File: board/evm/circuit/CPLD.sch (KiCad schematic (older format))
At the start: 1 part

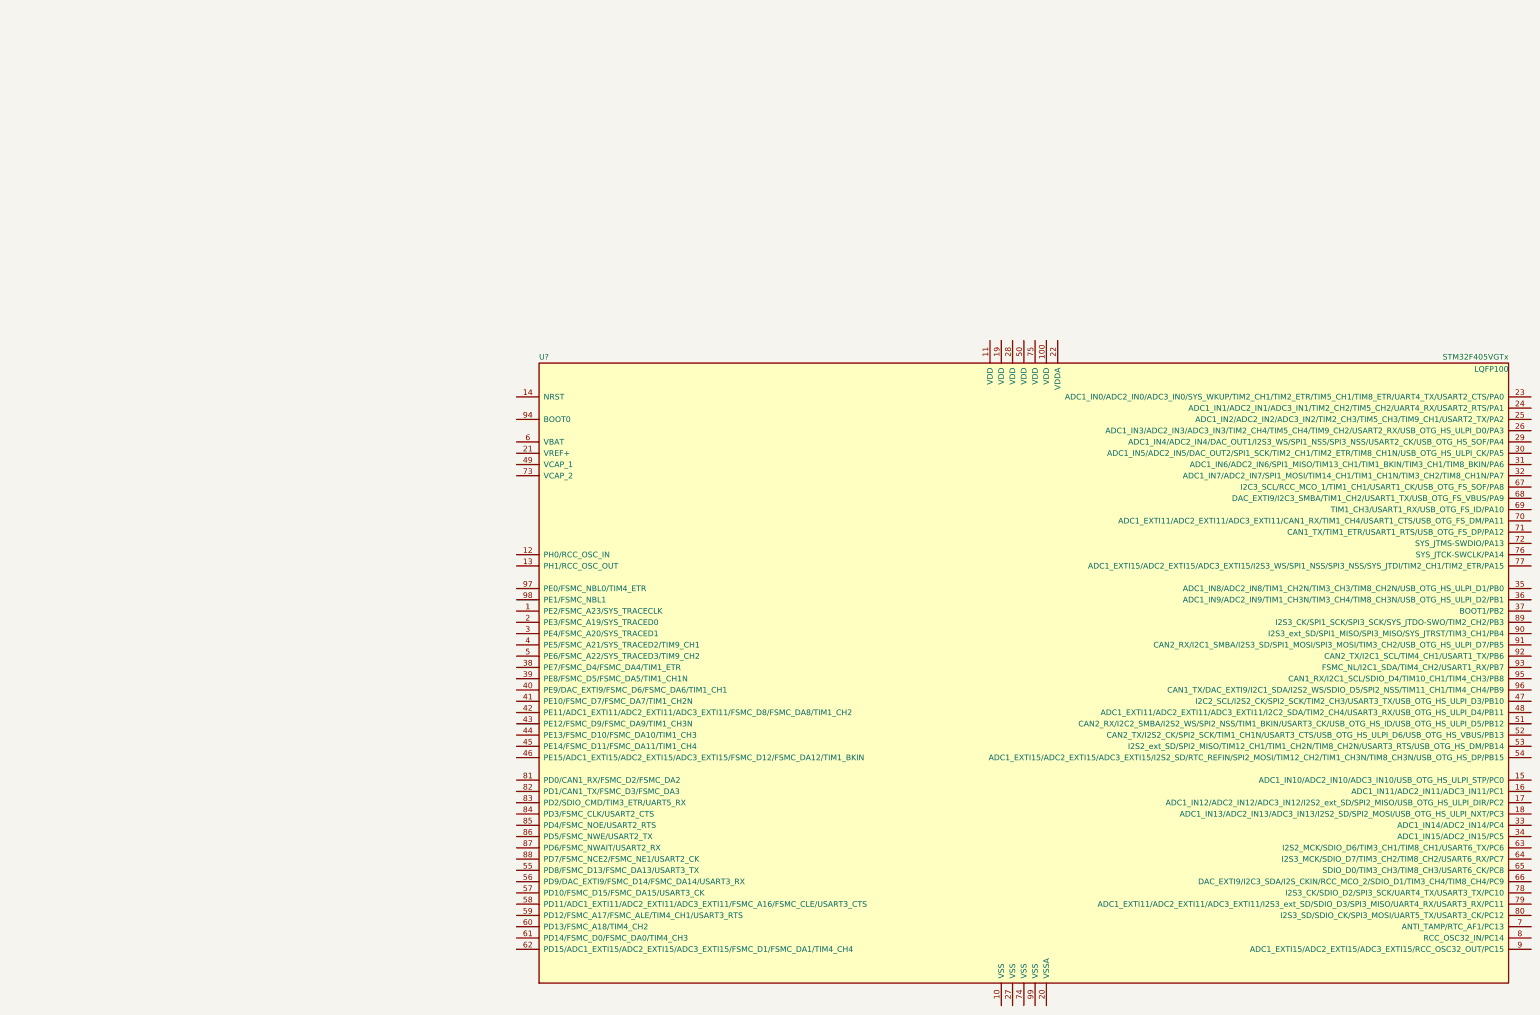
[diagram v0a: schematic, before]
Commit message: add cpld
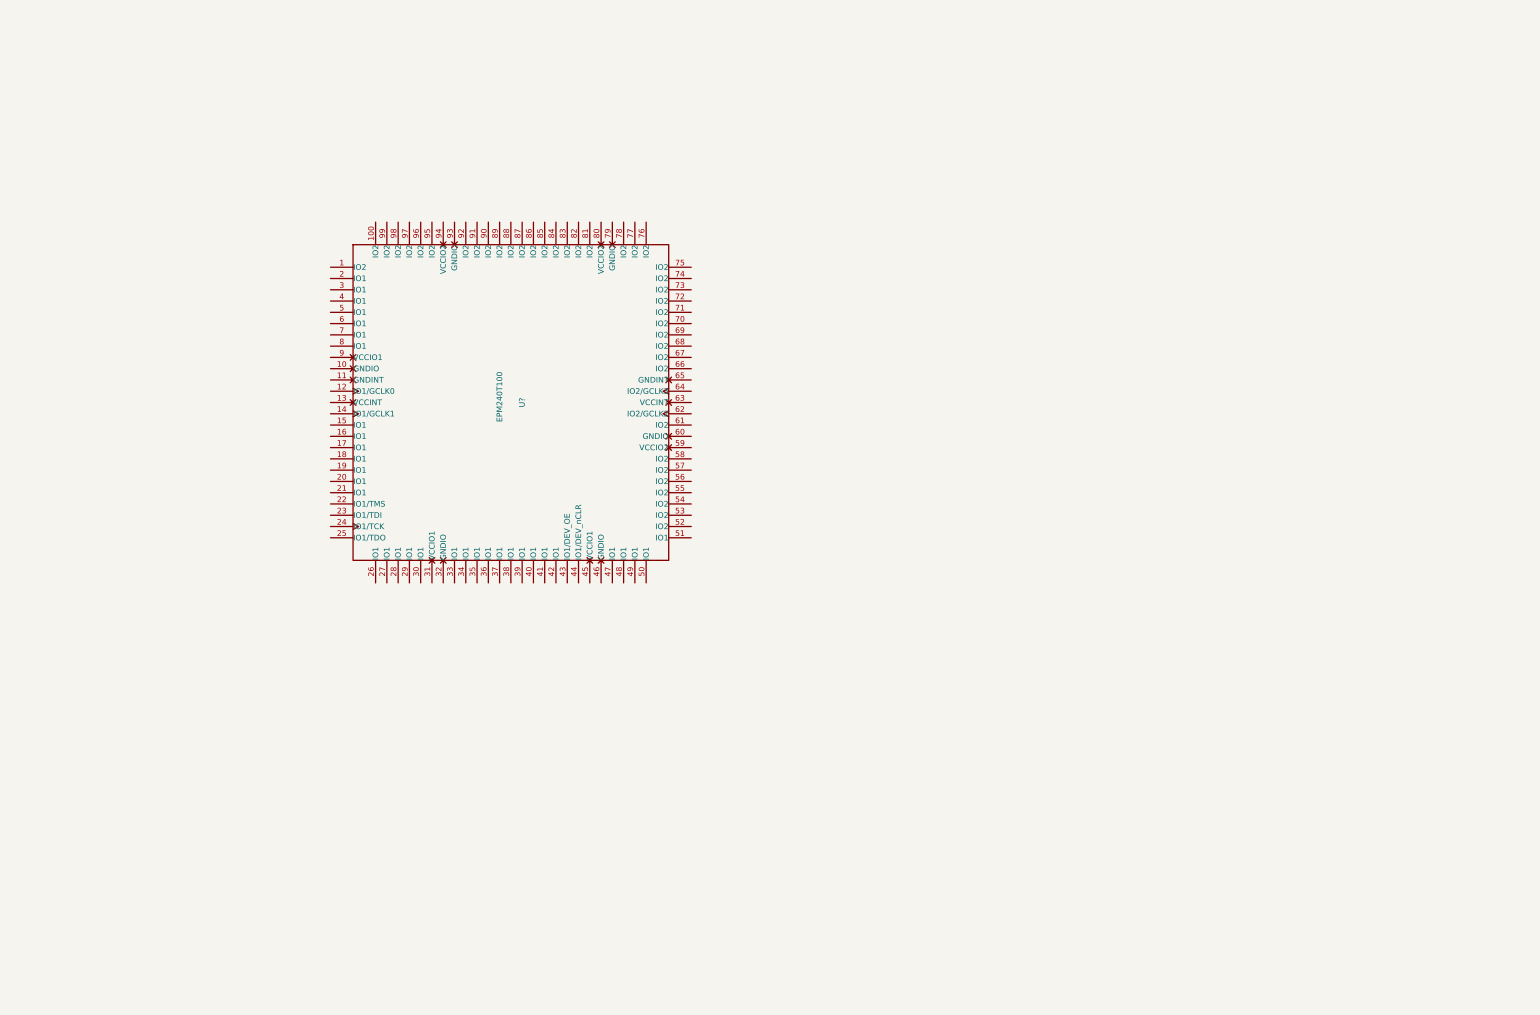
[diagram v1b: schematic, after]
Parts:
- removed U?: STM32F405VGTx, LQFP100, symbol STM32F405VGTx
- added U?: EPM240T100, symbol EPM240T100
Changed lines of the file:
@@
 $Descr A2 23386 16535
 encoding utf-8
-Sheet 2 4
+Sheet 4 4
 Title ""
 Date ""
@@
 $EndDescr
 $Comp
-L STM32F405VGTx U?
-U 1 1 5753F449
-P 9650 6400
-F 0 "U?" H 5350 9225 50  0000 L BNN
-F 1 "STM32F405VGTx" H 13950 9225 50  0000 R BNN
-F 2 "LQFP100" H 13950 9175 50  0000 R TNN
-F 3 "" H 9650 6400 50  0000 C CNN
-	1    9650 6400
+L EPM240T100 U?
+U 1 1 575650F8
+P 5100 3900
+F 0 "U?" V 5200 3850 50  0000 C CNN
+F 1 "EPM240T100" V 5000 3900 50  0000 C CNN
+F 2 "" V 4680 4400 30  0000 C CNN
+F 3 "" H 4750 4400 30  0000 C CNN
+	1    5100 3900
 	1    0    0    -1
 $EndComp

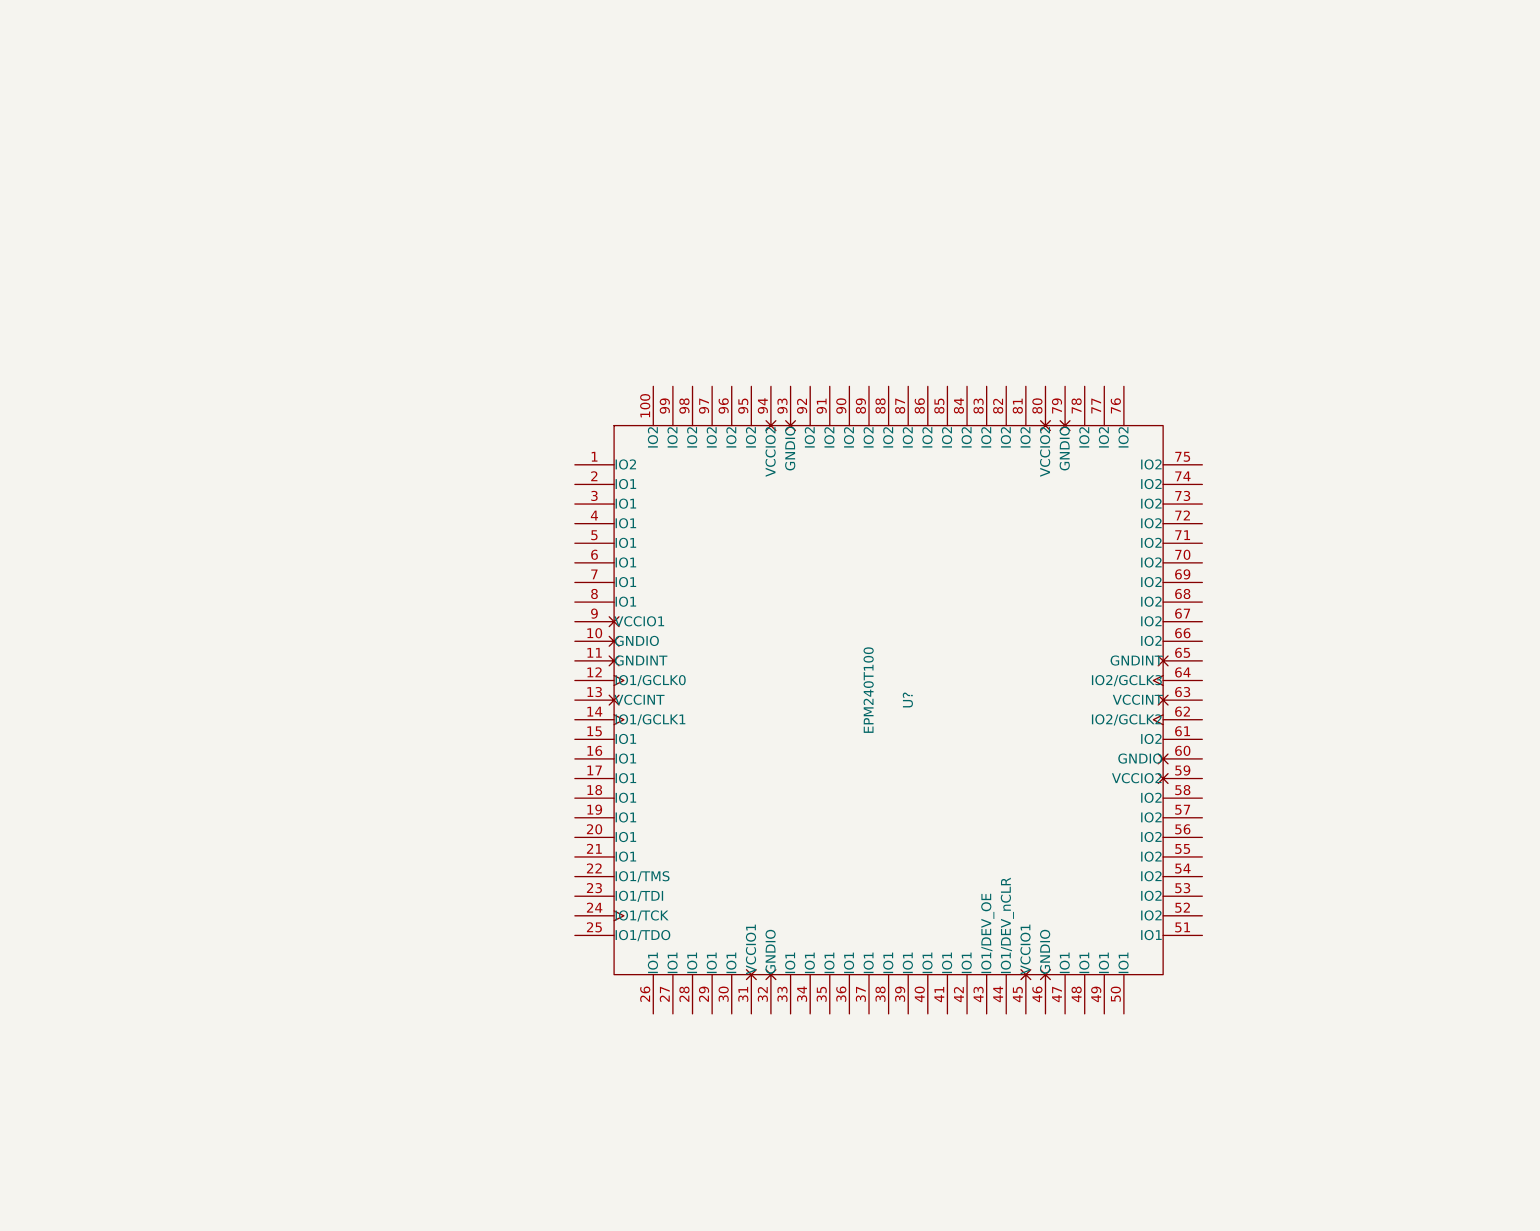
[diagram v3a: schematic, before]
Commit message: add more schs
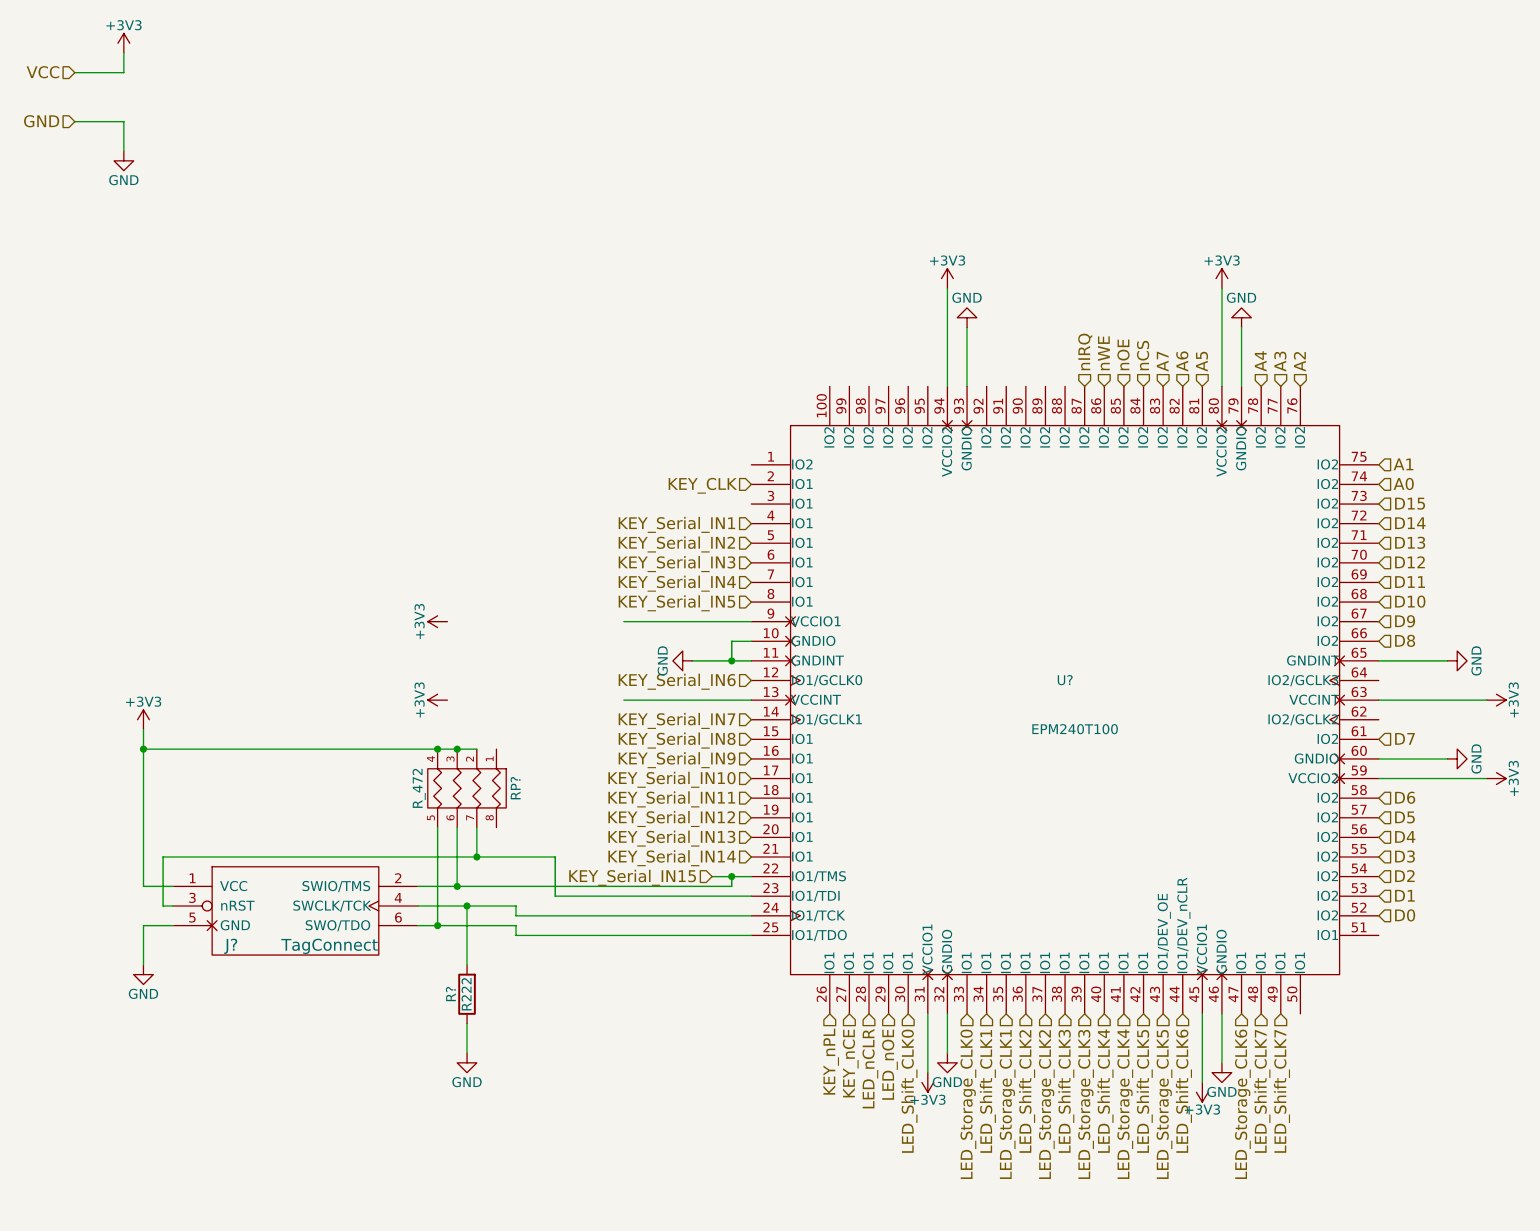
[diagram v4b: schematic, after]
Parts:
- added J?: TagConnect, symbol TagConnect
- added R?: R222, symbol R
- added RP?: R_472, symbol R_PACK4
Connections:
- net labels added: +3V3, A0, A1, A2, A3, A4, A5, A6, A7, D0, D1, D10, D11, D12, D13, D14, D15, D2, D3, D4, D5, D6, D7, D8, D9, GND, KEY_CLK, KEY_Serial_IN1, KEY_Serial_IN10, KEY_Serial_IN11, KEY_Serial_IN12, KEY_Serial_IN13, KEY_Serial_IN14, KEY_Serial_IN15, KEY_Serial_IN2, KEY_Serial_IN3, KEY_Serial_IN4, KEY_Serial_IN5, KEY_Serial_IN6, KEY_Serial_IN7, KEY_Serial_IN8, KEY_Serial_IN9, KEY_nCE, KEY_nPL, LED_Shift_CLK0, LED_Shift_CLK1, LED_Shift_CLK2, LED_Shift_CLK3, LED_Shift_CLK4, LED_Shift_CLK5, LED_Shift_CLK6, LED_Shift_CLK7, LED_Storage_CLK0, LED_Storage_CLK1, LED_Storage_CLK2, LED_Storage_CLK3, LED_Storage_CLK4, LED_Storage_CLK5, LED_Storage_CLK6, LED_nCLR, LED_nOE, VCC, nCS, nIRQ, nOE, nWE
- wire segments 0 -> 45
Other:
- moved on the sheet: U?

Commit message: evm sch design finished
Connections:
- net labels added: GPIO0, GPIO1, GPIO10, GPIO2, GPIO3, GPIO4, GPIO5, GPIO6, GPIO7, GPIO8, GPIO9
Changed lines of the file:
@@
 LIBS:contrib
 LIBS:valves
-LIBS:stm8
-LIBS:stm32
-LIBS:74xgxx
-LIBS:ac-dc
-LIBS:actel
 LIBS:Altera
-LIBS:analog_devices
-LIBS:battery_management
-LIBS:bbd
-LIBS:brooktre
-LIBS:cmos_ieee
-LIBS:dc-dc
-LIBS:diode
-LIBS:elec-unifil
-LIBS:ESD_Protection
-LIBS:ftdi
-LIBS:gennum
-LIBS:graphic
-LIBS:hc11
-LIBS:ir
-LIBS:Lattice
-LIBS:logo
-LIBS:maxim
-LIBS:microchip_dspic33dsc
-LIBS:microchip_pic10mcu
-LIBS:microchip_pic12mcu
-LIBS:microchip_pic16mcu
-LIBS:microchip_pic18mcu
-LIBS:microchip_pic32mcu
-LIBS:motor_drivers
-LIBS:msp430
-LIBS:nordicsemi
-LIBS:nxp_armmcu
-LIBS:onsemi
-LIBS:Oscillators
-LIBS:powerint
-LIBS:Power_Management
-LIBS:pspice
-LIBS:references
-LIBS:relays
-LIBS:rfcom
-LIBS:sensors
-LIBS:silabs
-LIBS:supertex
-LIBS:switches
-LIBS:transf
-LIBS:ttl_ieee
-LIBS:video
-LIBS:Worldsemi
-LIBS:Xicor
-LIBS:Zilog
+LIBS:my_kicad
 LIBS:oh-my-keyboard-cache
 EELAYER 25 0
@@
 $Descr A3 16535 11693
 encoding utf-8
-Sheet 4 11
+Sheet 4 12
 Title ""
 Date ""
@@
 	3200 5150 4400 5150
 Wire Wire Line
-	3400 4750 3400 4950
-Wire Wire Line
-	1400 4750 3400 4750
+	3400 4950 3400 4750
+Wire Wire Line
+	3400 4750 1400 4750
 Wire Wire Line
 	1400 4750 1400 5000
@@
 Text HLabel 6100 2350 1    60   Input ~ 0
 nIRQ
+Text HLabel 6000 2350 1    60   Input ~ 0
+GPIO0
+Text HLabel 5900 2350 1    60   Input ~ 0
+GPIO1
+Text HLabel 5800 2350 1    60   Input ~ 0
+GPIO2
+Text HLabel 5700 2350 1    60   Input ~ 0
+GPIO3
+Text HLabel 5600 2350 1    60   Input ~ 0
+GPIO4
+Text HLabel 5300 2350 1    60   Input ~ 0
+GPIO5
+Text HLabel 5200 2350 1    60   Input ~ 0
+GPIO6
+Text HLabel 5100 2350 1    60   Input ~ 0
+GPIO7
+Text HLabel 5000 2350 1    60   Input ~ 0
+GPIO8
+Text HLabel 4900 2350 1    60   Input ~ 0
+GPIO9
+Text HLabel 4800 2350 1    60   Input ~ 0
+GPIO10
 $EndSCHEMATC
